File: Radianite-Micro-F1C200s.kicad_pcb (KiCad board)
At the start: 2 copper layers, 60.2 x 27.5 mm, 73 parts, among them J1 USB_C_Receptacle_USB2.0, J2 USB_B_Micro, J3 AudioJack4, J4 Conn_01x04, J5 Micro_SD_Card_Det2, J6 Conn_02x14_Counter_Clockwise, SW1 SW_Push, U1 F1C200s, U2 CH340E, U3 JW5211, U4 JW5211, U5 JW5211, U6 W25Q256JWPIQ, Y1 24MHz

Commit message: 2.9 change on micro
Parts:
- moved C6 2.26 mm to (123.6, 108.8), turned to 0 degrees
- moved REF** 1.10 mm to (103.1, 125.9)
- moved C1 1.00 mm to (107.3, 121.4)
- moved C10 1.00 mm to (134.2, 113.6)
- moved C11 1.00 mm to (132.9, 113.8)
- moved C12 1.00 mm to (133.0, 115.2)
- moved C13 1.00 mm to (133.0, 115.9)
- moved C14 1.00 mm to (133.0, 116.6)
- moved C15 1.00 mm to (119.4, 115.2)
- moved C16 1.00 mm to (119.4, 114.5)
- moved C17 1.00 mm to (127.1, 125.1)
- moved C18 1.00 mm to (121.7, 125.8)
- moved C19 1.00 mm to (133.2, 126.4)
- moved C2 1.00 mm to (102.1, 117.8)
- moved C3 1.00 mm to (106.1, 123.7)
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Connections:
- J6 pad 21: unconnected-(J6-Pin_21-Pad21) -> /D10
- J6 pad 22: unconnected-(J6-Pin_22-Pad22) -> /D9
- J6 pad 24: unconnected-(J6-Pin_24-Pad24) -> +1V1
- J6 pad 25: unconnected-(J6-Pin_25-Pad25) -> +2V5
- U1 pad 15: unconnected-(U1A-PD9/LCD_D13/DA_LRCK/EINTD9-Pad15) -> /D9
- U1 pad 16: unconnected-(U1A-PD10/LCD_D14/DA_IN/EINTD10-Pad16) -> /D10
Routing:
- net /D9: track 0.00 -> 33.8 mm, vias 0 -> 5
- net +2V5: track 50.8 -> 71.1 mm, vias 5 -> 7
- net /D10: track 0.00 -> 17.6 mm, vias 0 -> 4
- net /D12: track 17.0 -> 33.5 mm
- net /D13: track 17.2 -> 32.9 mm
- net +3V3: track 17.4 -> 22.5 mm, vias 5 -> 6
- net +1V1: track 45.6 -> 49.5 mm
- net /D14: track 16.5 -> 19.7 mm
- net /D15: track 19.1 -> 21.0 mm
- net /D21: track 15.0 -> 16.0 mm
- net /D16: track 18.6 -> 19.5 mm
- net /D4: track 22.4 -> 21.8 mm
- net /D5: track 20.4 -> 19.8 mm
- net GND: track 37.0 -> 37.1 mm, vias 59 -> 91
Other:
- board size 60.2 x 27.5 mm -> 60 x 28 mm
- board text added: "1V1"
- board text added: "2V5"
- board text added: "32MB Flash"
- board text added: "D10"
- board text added: "D9"
- board text added: "F1C200s SoC"
- board text added: "r2.9"
- board text removed: "r2.5"

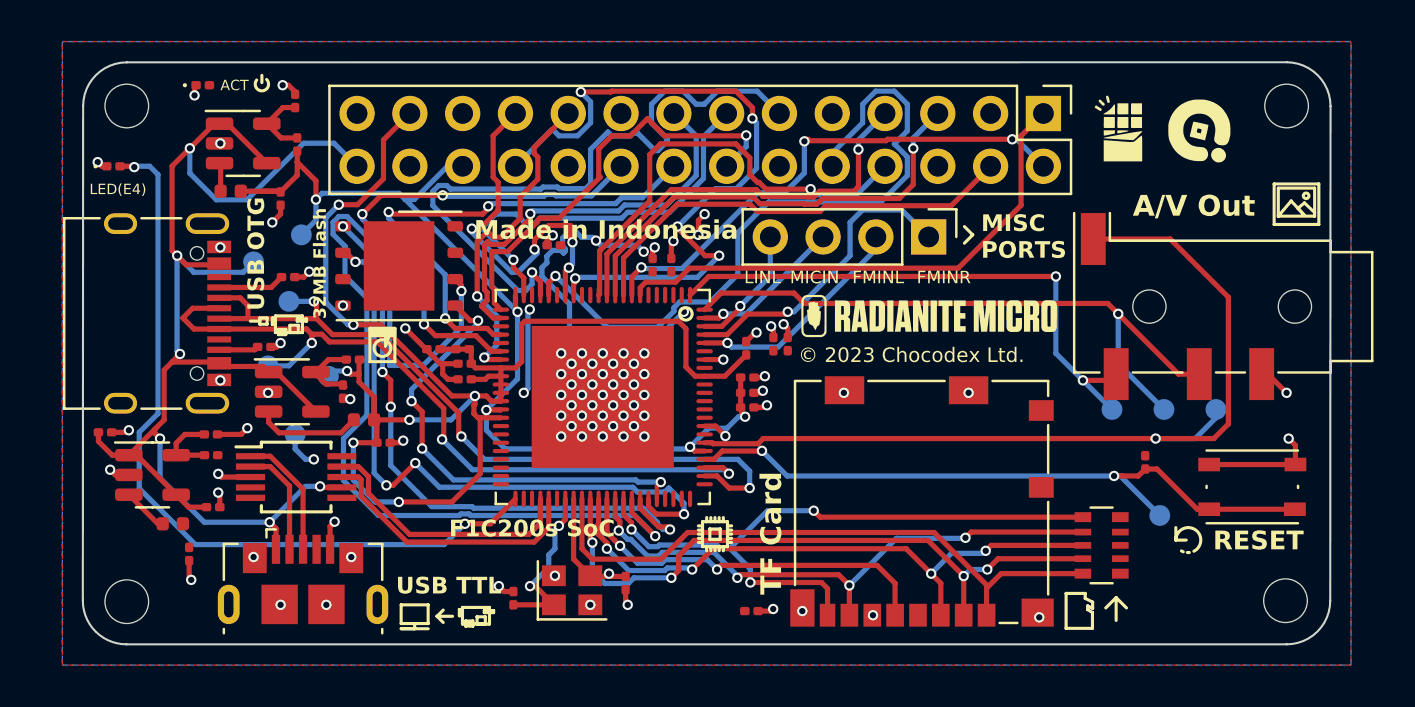
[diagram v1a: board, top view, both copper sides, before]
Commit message: revise to length tune track
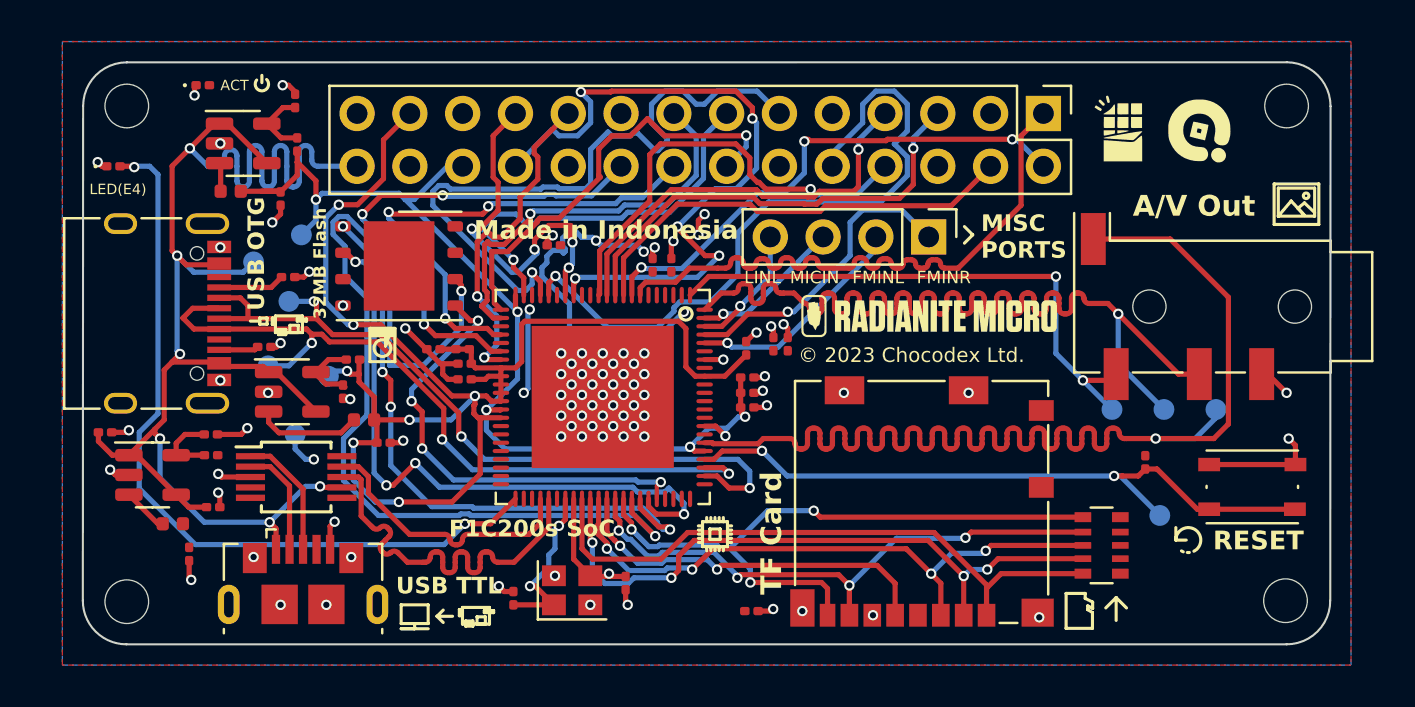
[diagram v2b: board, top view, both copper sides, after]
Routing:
- net /AV_VIDEO: track 43.1 -> 62.8 mm
- net /AV_R: track 31.3 -> 49.8 mm
- net VBUS: track 68.3 -> 76.6 mm
- net /SOC_TX: track 13.4 -> 19.6 mm
- net /D1: track 25.2 -> 29.1 mm
- net /SOC_RX: track 12.8 -> 13.3 mm
